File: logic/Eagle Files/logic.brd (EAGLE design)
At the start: 86 x 80.5 mm, 85 parts, among them J2 B2PS-VH(LF)(SN), J3 B2PS-VH(LF)(SN), J4 B2PS-VH(LF)(SN), J6 B2PS-VH(LF)(SN), Q4 STT4P3LLH6, T1 R-78E5.0-1.0, U1 9DoF IMU, U2 ICM-20948, U4 TLV70233DBVR, X1 MINI-USB_SHIELD5P4-32005-400, X2 C-GRID-05-15-91, X5 C-GRID-05-15-91, X7 SI-50170

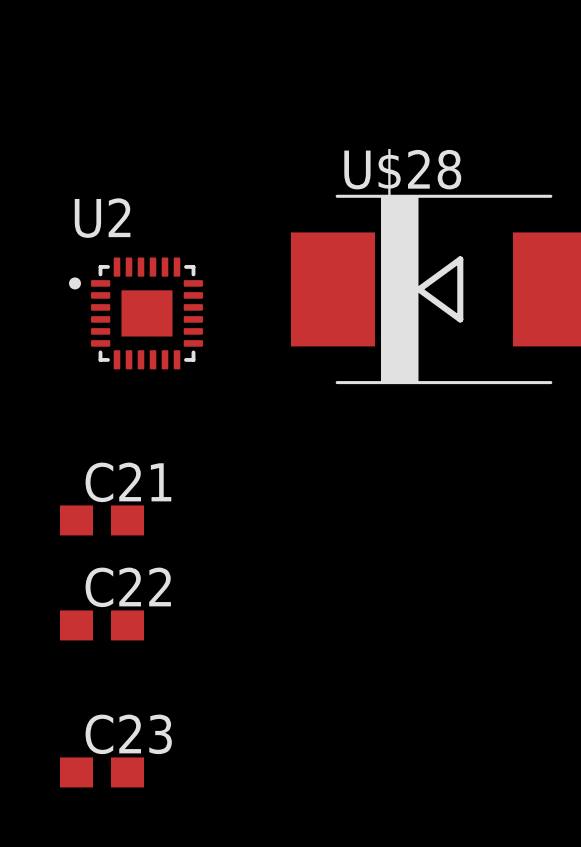
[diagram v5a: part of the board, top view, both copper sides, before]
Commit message: removed imu
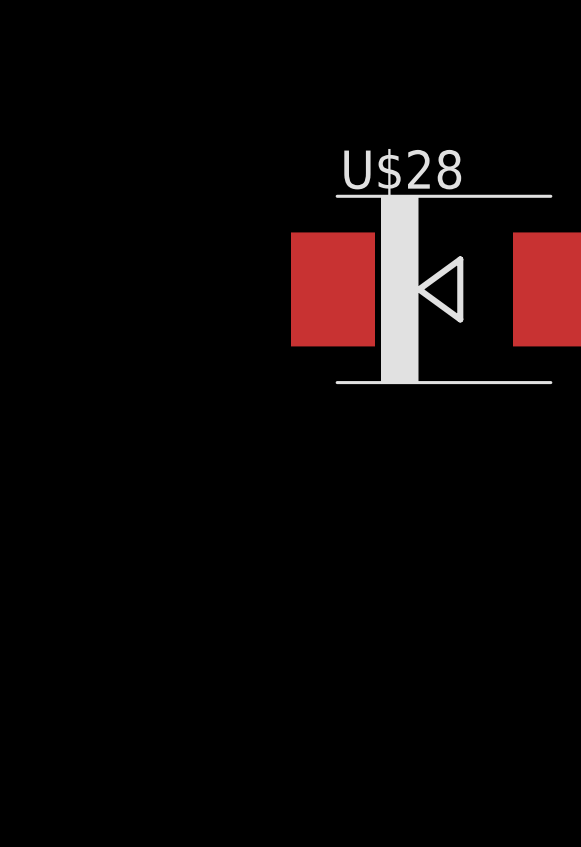
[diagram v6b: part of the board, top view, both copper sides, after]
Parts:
- removed C21, C22, C23: 0.1uF, rcl:C0603
- removed U2: ICM-20948, ICM-20948:QFN40P300X300X105-25N
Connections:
- removed net +1V8: C22.1, U2.22, U2.8
- removed net N$9: C23.1, U2.10
- net +3V3: no longer C21.1, U2.13
- net GND: no longer C21.2, C22.2, C23.2, U2.11, U2.18, U2.20, U2.25, U2.9
- net IMU_INT: no longer U2.12
- net SCL: no longer U2.23
- net SDA: no longer U2.24

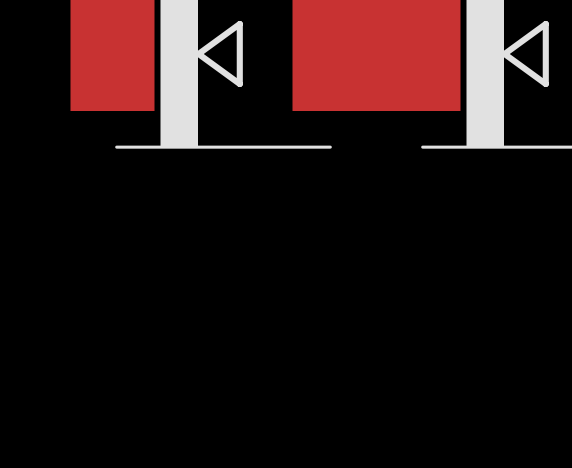
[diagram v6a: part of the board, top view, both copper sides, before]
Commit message: added IMA198 to sch
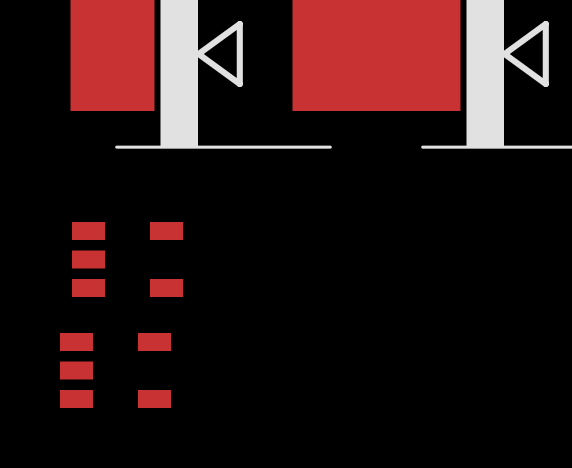
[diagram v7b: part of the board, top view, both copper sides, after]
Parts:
- added U$29, U$30: IMA198, IGVC-Sensor:SOT-23-5
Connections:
- new net +5V_ENCODER1: U$29.P$5
- new net +5V_ENDODER2: U$30.P$5
- new net ENCODER1_SENSE: U$29.P$1
- new net ENCODER2_SENSE: U$30.P$1
- net +5V: now also U$29.P$3, U$29.P$4, U$30.P$3, U$30.P$4
- net GND: now also U$29.P$2, U$30.P$2

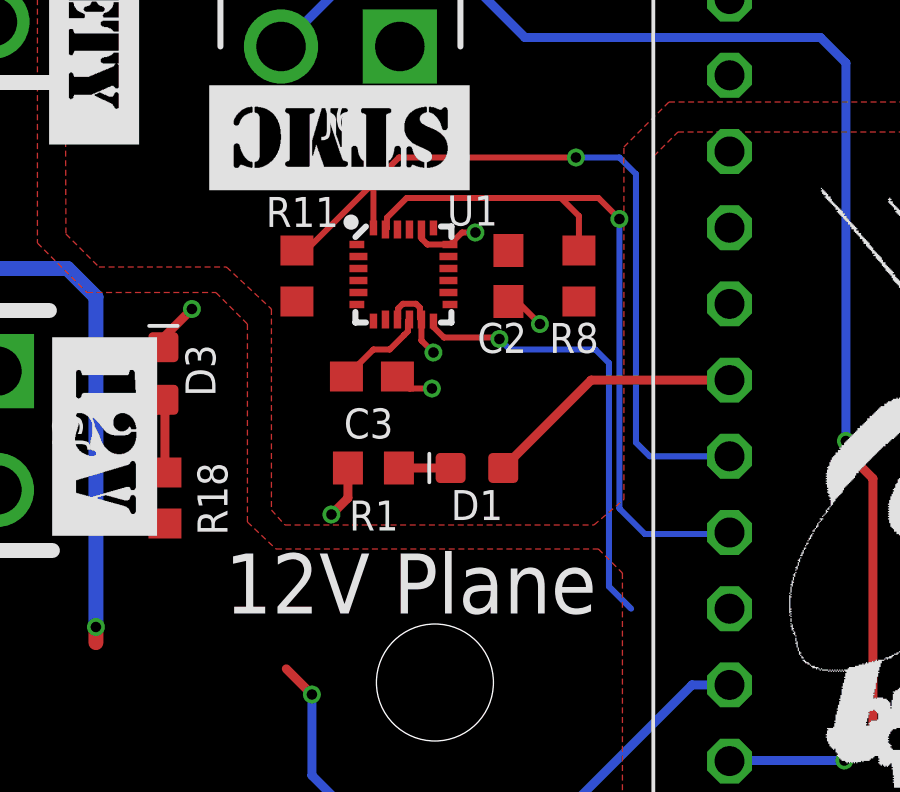
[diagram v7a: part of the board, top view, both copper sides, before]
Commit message: removed IMU from sch
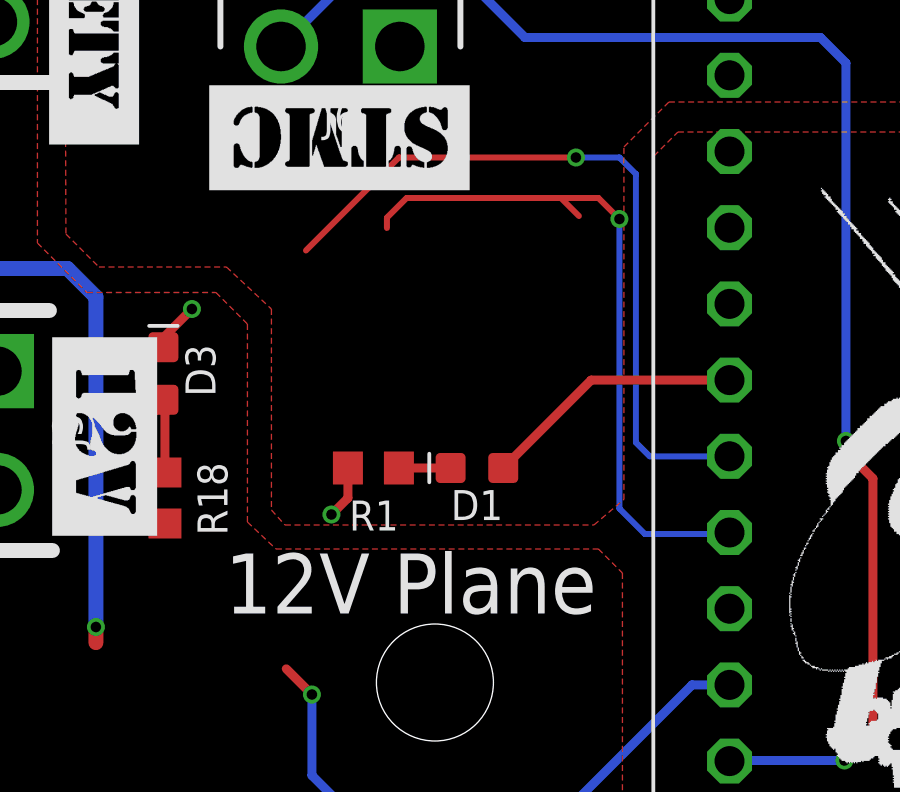
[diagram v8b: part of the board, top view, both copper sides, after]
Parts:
- removed C2, C3: 0.1uF, rcl:C0603
- removed R11, R8: 4.7k, rcl:R0603
- removed U1: 9DoF IMU, SparkFun-Sensors:QFN24-3X3
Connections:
- removed net GYRO_INT: U1.12
- removed net REGOUT_C: C3.1, U1.10
- net +3V3: no longer C2.1, R11.2, R8.2, U1.1, U1.13, U1.22, U1.8
- net GND: no longer C2.2, C3.2, U1.11, U1.18, U1.20, U1.9
- net SCL: no longer R8.1, U1.23
- net SDA: no longer R11.1, U1.24
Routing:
- net GYRO_INT: track 15.0 -> 0.00 mm, vias 1 -> 0
- net GND: track 36.1 -> 28.1 mm, vias 19 -> 15
- net REGOUT_C: track 3.09 -> 0.00 mm
- net SDA: track 26.6 -> 24.8 mm
- net SCL: track 24.4 -> 23.2 mm
